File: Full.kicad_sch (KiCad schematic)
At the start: 0 parts

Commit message: made Full Op-Amp
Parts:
- added C1, C10, C11, C12, C13, C14, C15, C16, C2, C3, C4, C5, C6, C7, C8, C9: C, Capacitor_THT:C_Disc_D3.0mm_W2.0mm_P2.50mm, symbol Device:C
- added J1, J10, J11, J12, J13, J14, J15, J16, J17, J18, J19, J2, J20, J21, J22, J23, J24, J25, J26, J27, J28, J29, J3, J30, J31, J32, J33, J34, J35, J36, J37, J38, J4, J5, J6, J7, J8, J9: Conn_01x04_Pin, Connector_PinHeader_2.54mm:PinHeader_1x04_P2.54mm_Vertical, symbol Connector:Conn_01x04_Pin
- added R1, R10, R11, R12, R13, R14, R15, R16, R2, R3, R4, R5, R6, R7, R8, R9: R_US, Resistor_THT:R_Axial_DIN0207_L6.3mm_D2.5mm_P10.16mm_Horizontal, symbol Device:R_US
- added U1: LM358, symbol Amplifier_Operational:LM358
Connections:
- new net: J16.1 (Pin_1), J16.2 (Pin_2), J16.3 (Pin_3), J16.4 (Pin_4), R6.1
- new net: J36.1 (Pin_1), J36.2 (Pin_2), J36.3 (Pin_3), J36.4 (Pin_4), R16.1
- new net: C5.1, C6.1, C7.1, C8.1, J19.1 (Pin_1), J19.2 (Pin_2), J19.3 (Pin_3), J19.4 (Pin_4), R5.2, R6.2, R7.2, R8.2, U1.2 (-)
- new net: C13.1, C14.1, C15.1, C16.1, J37.1 (Pin_1), J37.2 (Pin_2), J37.3 (Pin_3), J37.4 (Pin_4), R13.2, R14.2, R15.2, R16.2, U1.6 (-)
- new net: C16.2, J27.1 (Pin_1), J27.2 (Pin_2), J27.3 (Pin_3), J27.4 (Pin_4)
- new net: J29.1 (Pin_1), J29.2 (Pin_2), J29.3 (Pin_3), J29.4 (Pin_4), R9.1
- new net: C10.1, C11.1, C12.1, C9.1, J38.1 (Pin_1), J38.2 (Pin_2), J38.3 (Pin_3), J38.4 (Pin_4), R10.2, R11.2, R12.2, R9.2, U1.5 (+)
- new net: C12.2, J23.1 (Pin_1), J23.2 (Pin_2), J23.3 (Pin_3), J23.4 (Pin_4)
- new net: J14.1 (Pin_1), J14.2 (Pin_2), J14.3 (Pin_3), J14.4 (Pin_4), R8.1
- new net: J31.1 (Pin_1), J31.2 (Pin_2), J31.3 (Pin_3), J31.4 (Pin_4), R11.1
- new net: J28.1 (Pin_1), J28.2 (Pin_2), J28.3 (Pin_3), J28.4 (Pin_4), U1.7
- new net: J33.1 (Pin_1), J33.2 (Pin_2), J33.3 (Pin_3), J33.4 (Pin_4), R13.1
- new net: J15.1 (Pin_1), J15.2 (Pin_2), J15.3 (Pin_3), J15.4 (Pin_4), R7.1
- new net: C7.2, J12.1 (Pin_1), J12.2 (Pin_2), J12.3 (Pin_3), J12.4 (Pin_4)
- new net: C1.1, C2.1, C3.1, C4.1, J18.1 (Pin_1), J18.2 (Pin_2), J18.3 (Pin_3), J18.4 (Pin_4), R1.2, R2.2, R3.2, R4.2, U1.3 (+)
- new net: C2.2, J3.1 (Pin_1), J3.2 (Pin_2), J3.3 (Pin_3), J3.4 (Pin_4)
- new net: C8.2, J13.1 (Pin_1), J13.2 (Pin_2), J13.3 (Pin_3), J13.4 (Pin_4)
- new net: C13.2, J24.1 (Pin_1), J24.2 (Pin_2), J24.3 (Pin_3), J24.4 (Pin_4)
- new net: J7.1 (Pin_1), J7.2 (Pin_2), J7.3 (Pin_3), J7.4 (Pin_4), R3.1
- new net: J32.1 (Pin_1), J32.2 (Pin_2), J32.3 (Pin_3), J32.4 (Pin_4), R12.1
- new net: C5.2, J10.1 (Pin_1), J10.2 (Pin_2), J10.3 (Pin_3), J10.4 (Pin_4)
- new net: C14.2, J25.1 (Pin_1), J25.2 (Pin_2), J25.3 (Pin_3), J25.4 (Pin_4)
- new net: C10.2, J21.1 (Pin_1), J21.2 (Pin_2), J21.3 (Pin_3), J21.4 (Pin_4)
- new net: J5.1 (Pin_1), J5.2 (Pin_2), J5.3 (Pin_3), J5.4 (Pin_4), R1.1
- new net: J17.1 (Pin_1), J17.2 (Pin_2), J17.3 (Pin_3), J17.4 (Pin_4), R5.1
- new net: J6.1 (Pin_1), J6.2 (Pin_2), J6.3 (Pin_3), J6.4 (Pin_4), R2.1
- new net: C15.2, J26.1 (Pin_1), J26.2 (Pin_2), J26.3 (Pin_3), J26.4 (Pin_4)
- new net: C3.2, J2.1 (Pin_1), J2.2 (Pin_2), J2.3 (Pin_3), J2.4 (Pin_4)
- new net: C9.2, J20.1 (Pin_1), J20.2 (Pin_2), J20.3 (Pin_3), J20.4 (Pin_4)
- new net: J9.1 (Pin_1), J9.2 (Pin_2), J9.3 (Pin_3), J9.4 (Pin_4), U1.1
- new net: C6.2, J11.1 (Pin_1), J11.2 (Pin_2), J11.3 (Pin_3), J11.4 (Pin_4)
- new net: C4.2, J1.1 (Pin_1), J1.2 (Pin_2), J1.3 (Pin_3), J1.4 (Pin_4)
- new net: J35.1 (Pin_1), J35.2 (Pin_2), J35.3 (Pin_3), J35.4 (Pin_4), R15.1
- new net: J8.1 (Pin_1), J8.2 (Pin_2), J8.3 (Pin_3), J8.4 (Pin_4), R4.1
- new net: C1.2, J4.1 (Pin_1), J4.2 (Pin_2), J4.3 (Pin_3), J4.4 (Pin_4)
- new net: J34.1 (Pin_1), J34.2 (Pin_2), J34.3 (Pin_3), J34.4 (Pin_4), R14.1
- new net: C11.2, J22.1 (Pin_1), J22.2 (Pin_2), J22.3 (Pin_3), J22.4 (Pin_4)
- new net: J30.1 (Pin_1), J30.2 (Pin_2), J30.3 (Pin_3), J30.4 (Pin_4), R10.1
- new net +15V: U1.8 (V+)
- new net -15V: U1.4 (V-)
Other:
- note added: "Op-Amp 1"
- note added: "Op-Amp 2"
- note added: "Power Supply"
- title: (none) -> Full Op-Amp

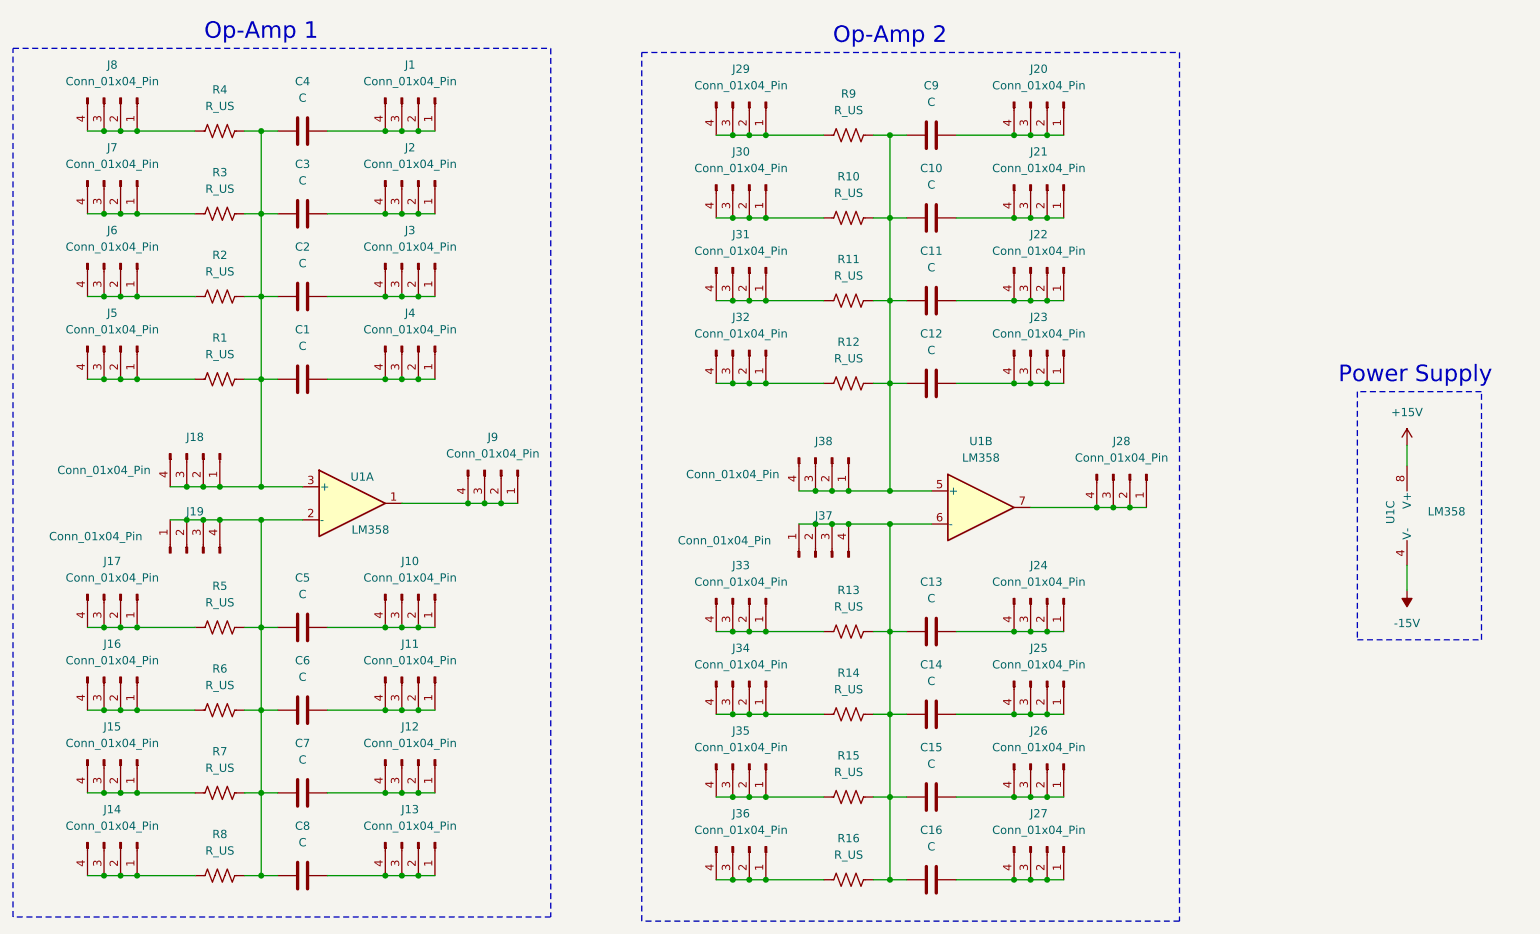
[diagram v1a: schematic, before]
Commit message: added inverting ckt
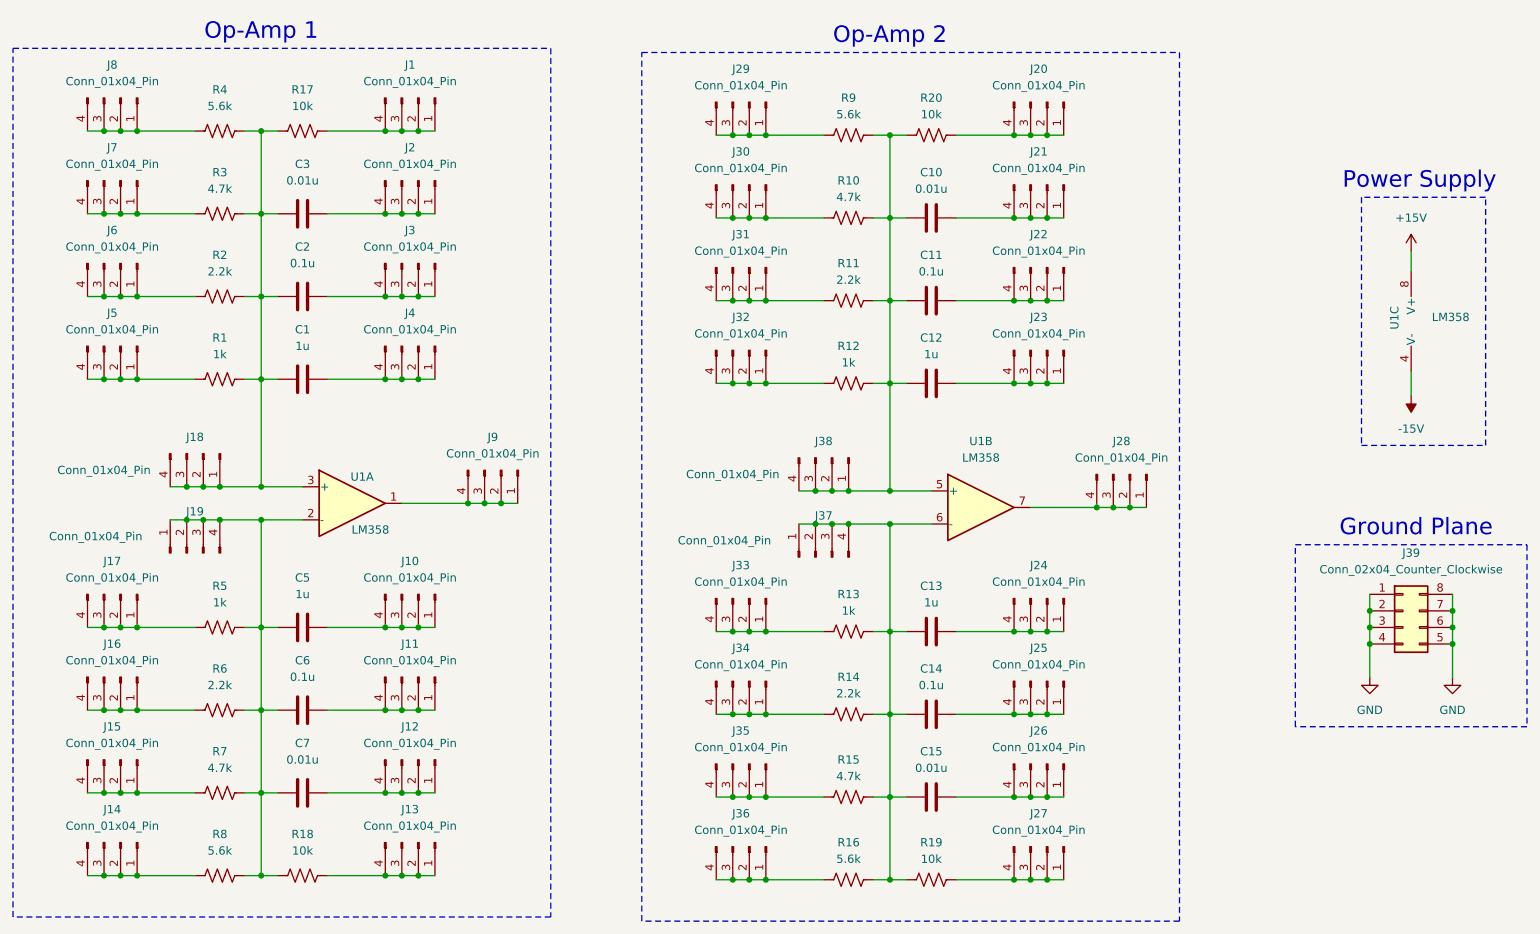
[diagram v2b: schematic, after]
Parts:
- removed C16, C4, C8, C9: C, Capacitor_THT:C_Disc_D3.0mm_W2.0mm_P2.50mm, symbol Device:C
- added J39: Conn_02x04_Counter_Clockwise, Connector_PinHeader_2.54mm:PinHeader_2x04_P2.54mm_Vertical, symbol Connector_Generic:Conn_02x04_Counter_Clockwise
- added R17, R18, R19, R20: 10k, Resistor_THT:R_Axial_DIN0207_L6.3mm_D2.5mm_P10.16mm_Horizontal, symbol Device:R_US
- C1, C12, C13, C5: value C -> 1u; footprint Capacitor_THT:C_Disc_D3.0mm_W2.0mm_P2.50mm -> Capacitor_THT:C_Disc_D5.0mm_W2.5mm_P5.00mm
- C10, C15, C3, C7: value C -> 0.01u; footprint Capacitor_THT:C_Disc_D3.0mm_W2.0mm_P2.50mm -> Capacitor_THT:C_Disc_D5.0mm_W2.5mm_P5.00mm
- C11, C14, C2, C6: value C -> 0.1u; footprint Capacitor_THT:C_Disc_D3.0mm_W2.0mm_P2.50mm -> Capacitor_THT:C_Disc_D5.0mm_W2.5mm_P5.00mm
- R1, R12, R13, R5: value R_US -> 1k
- R10, R15, R3, R7: value R_US -> 4.7k
- R11, R14, R2, R6: value R_US -> 2.2k
- R16, R4, R8, R9: value R_US -> 5.6k
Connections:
- net at C5.1, C6.1, C7.1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: now also R18.1
- net at C13.1, C14.1, C15.1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: now also R19.1
- net at J27.1 (Pin_1), J27.2 (Pin_2), J27.3 (Pin_3)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: now also R19.2
- net at C10.1, C11.1, C12.1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: now also R20.1
- net at C1.1, C2.1, C3.1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: now also R17.1
- net at J13.1 (Pin_1), J13.2 (Pin_2), J13.3 (Pin_3)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: now also R18.2
- net at J20.1 (Pin_1), J20.2 (Pin_2), J20.3 (Pin_3)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: now also R20.2
- net at J1.1 (Pin_1), J1.2 (Pin_2), J1.3 (Pin_3)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: now also R17.2
- new net GND: J39.1 (Pin_1), J39.2 (Pin_2), J39.3 (Pin_3), J39.4 (Pin_4), J39.5 (Pin_5), J39.6 (Pin_6), J39.7 (Pin_7), J39.8 (Pin_8)
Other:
- note added: "Ground Plane"
- moved on the sheet: U1C

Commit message: Floor Planning 50%
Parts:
- removed J39: Conn_02x04_Counter_Clockwise, Connector_PinHeader_2.54mm:PinHeader_2x04_P2.54mm_Vertical, symbol Connector_Generic:Conn_02x04_Counter_Clockwise
- C1, C10, C11, C12, C13, C14, C15, C2, C3, C5, C6, C7: footprint Capacitor_THT:C_Disc_D5.0mm_W2.5mm_P5.00mm -> Capacitor_SMD:C_0805_2012Metric_Pad1.18x1.45mm_HandSolder
- U1: footprint (none) -> Package_DIP:DIP-8_W7.62mm_LongPads
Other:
- note removed: "Ground Plane"

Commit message: Completed V1
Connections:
- net at C5.1, C6.1, C7.1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: now also U1.3 (+); no longer U1.2 (-)
- net at C10.1, C11.1, C12.1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: now also U1.6 (-); no longer U1.5 (+)
- net at C13.1, C14.1, C15.1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: now also U1.5 (+); no longer U1.6 (-)
- net at C1.1, C2.1, C3.1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: now also U1.2 (-); no longer U1.3 (+)
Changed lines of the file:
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@@
 		(lib_id "Amplifier_Operational:LM358")
 		(at 180.34 95.885 0)
+		(mirror x)
 		(unit 2)
 		(exclude_from_sim no)
@@
 		(on_board yes)
 		(dnp no)
-		(fields_autoplaced yes)
 		(property "Reference" "U1"
-			(at 180.34 85.725 0)
+			(at 180.34 106.045 0)
 			(effects
 				(font
@@
 		)
 		(property "Value" "LM358"
-			(at 180.34 88.265 0)
+			(at 180.34 103.505 0)
 			(effects
 				(font
@@
 		(lib_id "Amplifier_Operational:LM358")
 		(at 83.82 95.25 0)
+		(mirror x)
 		(unit 1)
 		(exclude_from_sim no)
@@
 		(dnp no)
 		(property "Reference" "U1"
-			(at 85.344 91.186 0)
+			(at 85.344 99.314 0)
 			(effects
 				(font
@@
 		)
 		(property "Value" "LM358"
-			(at 86.614 99.314 0)
-			(effects
-				(font
+			(at 86.614 91.186 0)
+			(effects
+				(font
